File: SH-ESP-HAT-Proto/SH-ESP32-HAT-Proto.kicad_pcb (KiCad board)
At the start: 2 copper layers, 83 x 55.5 mm, 459 parts, among them J301 Conn_01x02, J302 GPIO, J304 Conn_01x02, J306 Conn_01x04, J307 GPIO, P301 Conn_01x01_Male, P302 Conn_01x01_Male, P303 Conn_01x01_Male, P304 Conn_01x01_Male, P305 Conn_01x01_Male, P306 Conn_01x01_Male, P307 Conn_01x01_Male, P308 Conn_01x01_Male, P309 Conn_01x01_Male, P310 Conn_01x01_Male, P311 Conn_01x01_Male, P312 Conn_01x01_Male, P313 Conn_01x01_Male, P314 Conn_01x01_Male, P315 Conn_01x01_Male, P316 Conn_01x01_Male, P317 Conn_01x01_Male, P319 Conn_01x01_Male, P320 Conn_01x01_Male, P322 Conn_01x01_Male, P323 Conn_01x01_Male, P324 Conn_01x01_Male, P325 Conn_01x01_Male, P326 Conn_01x01_Male, P327 Conn_01x01_Male, P328 Conn_01x01_Male, P329 Conn_01x01_Male, P330 Conn_01x01_Male

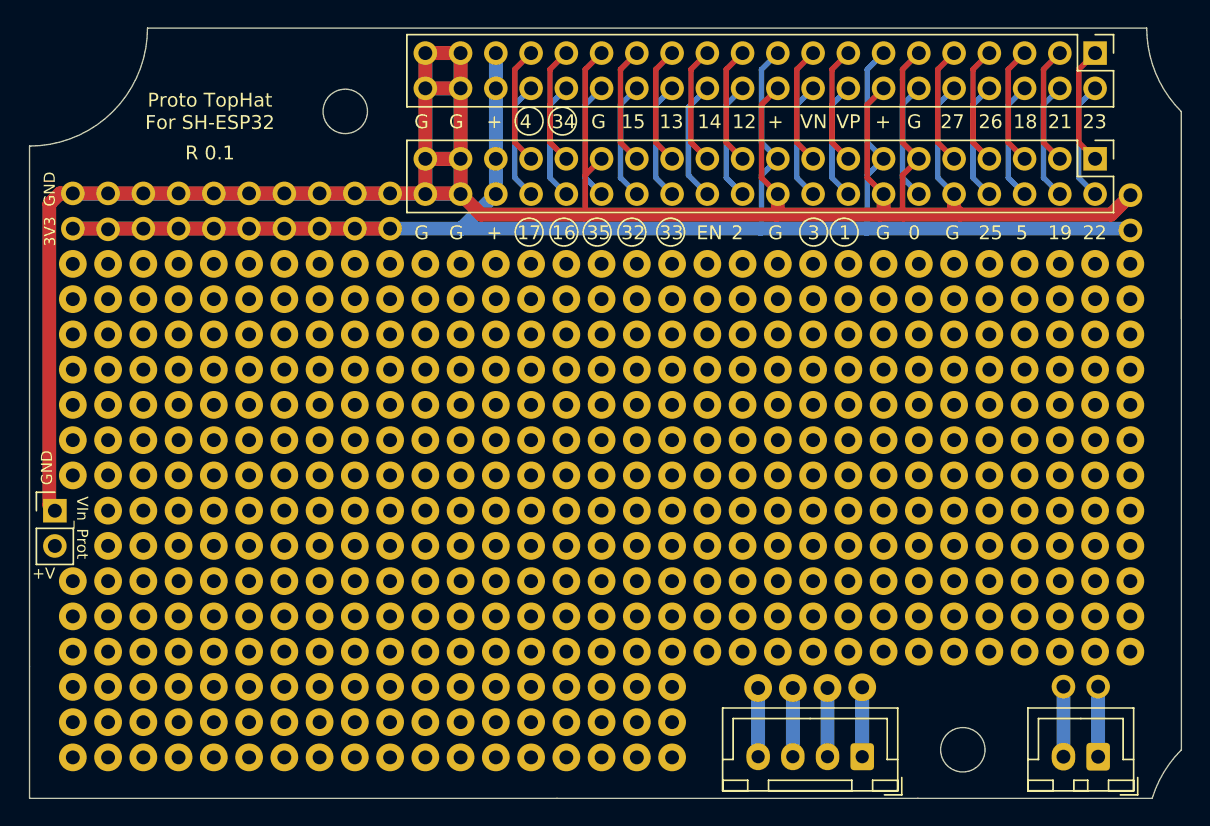
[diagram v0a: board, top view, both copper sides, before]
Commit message: Update HAT-Proto to V0.3  Pin header locs and fix outline for box corners
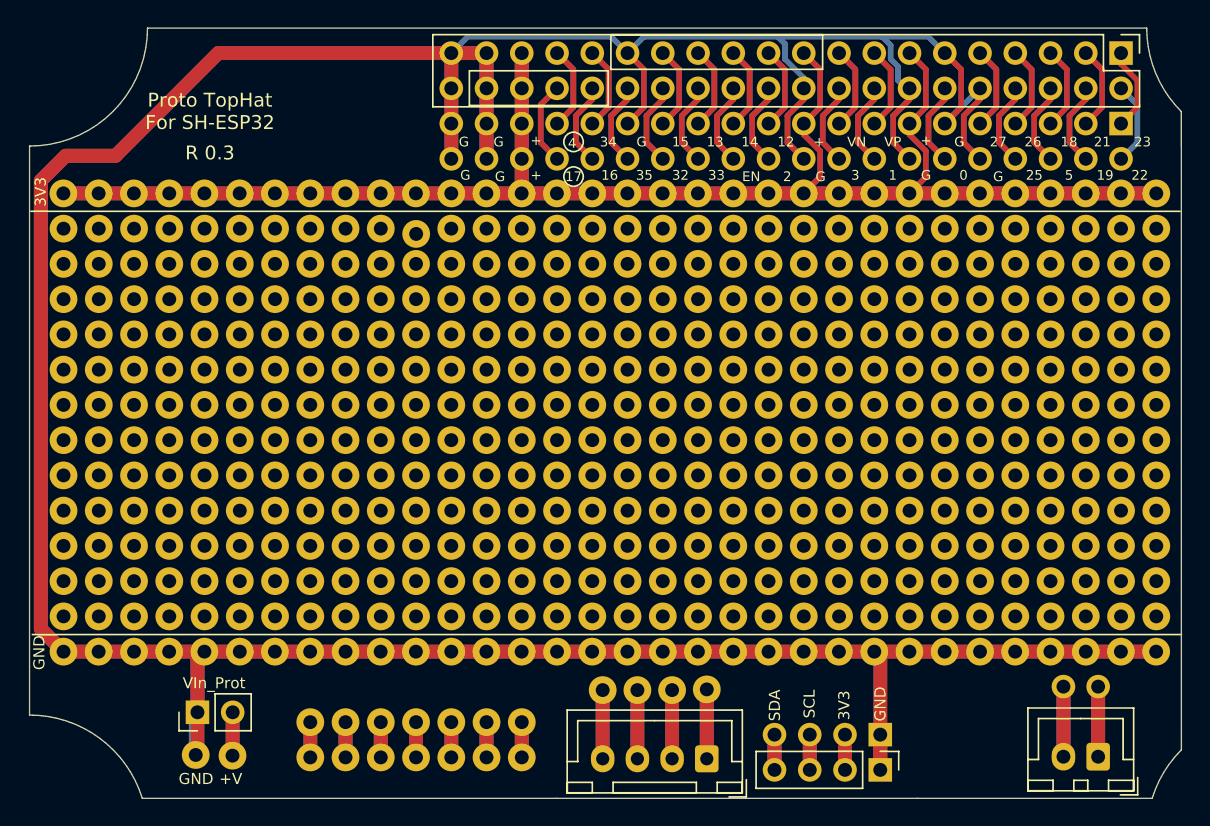
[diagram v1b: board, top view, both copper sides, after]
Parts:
- removed P307, P308, P309, P310, P311, P312, P313, P314, P315, P316, P317, P319, P320, P322, P323, P324, P325, P326, P327, P328, P329, P330: Conn_01x01_Male, ESP32-HAT:ProtoPad-Drill1mm
- removed the REF** at (97.2, 107.1)
- removed the REF** at (158.2, 102.0)
- removed the REF** at (145.5, 102.0)
- removed the REF** at (148.0, 102.0)
- removed the REF** at (153.1, 102.0)
- removed the REF** at (150.5, 102.0)
- removed the REF** at (142.9, 102.0)
- removed the REF** at (165.8, 102.0)
- removed the REF** at (99.7, 102.0)
- removed the REF** at (94.7, 102.0)
- removed the REF** at (102.3, 102.0)
- removed the REF** at (92.1, 102.0)
- removed the REF** at (163.2, 102.0)
- removed the REF** at (97.2, 102.0)
- removed the REF** at (155.6, 102.0)
- removed the REF** at (160.7, 102.0)
- removed the REF** at (125.1, 99.4)
- removed the REF** at (117.5, 99.4)
- removed the REF** at (122.6, 99.4)
- removed the REF** at (137.8, 99.4)
- removed the REF** at (135.3, 99.4)
- removed the REF** at (104.8, 109.6)
- removed the REF** at (120.1, 99.4)
- removed the REF** at (127.7, 99.4)
- removed the REF** at (130.2, 99.4)
- removed the REF** at (115.0, 99.4)
- removed the REF** at (112.4, 99.4)
- removed the REF** at (104.8, 99.4)
- removed the REF** at (109.9, 99.4)
- removed the REF** at (132.8, 99.4)
- removed the REF** at (140.4, 99.4)
- removed the REF** at (107.4, 99.4)
- removed the REF** at (158.2, 99.4)
- removed the REF** at (145.5, 99.4)
- removed the REF** at (148.0, 99.4)
- removed the REF** at (153.1, 99.4)
- removed the REF** at (150.5, 99.4)
- removed the REF** at (142.9, 99.4)
- removed the REF** at (165.8, 99.4)
- removed the REF** at (99.7, 99.4)
- removed the REF** at (94.7, 99.4)
- removed the REF** at (102.3, 99.4)
- removed the REF** at (132.8, 109.6)
- removed the REF** at (92.1, 99.4)
- removed the REF** at (163.2, 99.4)
- removed the REF** at (97.2, 99.4)
- removed the REF** at (155.6, 99.4)
- removed the REF** at (160.7, 99.4)
- removed the REF** at (125.1, 96.9)
- removed the REF** at (117.5, 96.9)
- removed the REF** at (122.6, 96.9)
- removed the REF** at (137.8, 96.9)
- removed the REF** at (135.3, 96.9)
- removed the REF** at (120.1, 96.9)
- removed the REF** at (127.7, 96.9)
- removed the REF** at (130.2, 96.9)
- removed the REF** at (115.0, 96.9)
- removed the REF** at (112.4, 96.9)
- removed the REF** at (104.8, 96.9)
- removed the REF** at (109.9, 96.9)
- removed the REF** at (132.8, 96.9)
- removed the REF** at (140.4, 96.9)
- removed the REF** at (107.4, 96.9)
- removed the REF** at (158.2, 96.9)
- removed the REF** at (145.5, 96.9)
- removed the REF** at (148.0, 96.9)
- removed the REF** at (153.1, 96.9)
- removed the REF** at (150.5, 96.9)
- removed the REF** at (142.9, 96.9)
- removed the REF** at (165.8, 96.9)
- removed the REF** at (99.7, 96.9)
- removed the REF** at (94.7, 96.9)
- removed the REF** at (102.3, 96.9)
- removed the REF** at (135.3, 109.6)
- removed the REF** at (92.1, 96.9)
- removed the REF** at (163.2, 96.9)
- removed the REF** at (97.2, 96.9)
- removed the REF** at (155.6, 96.9)
- removed the REF** at (160.7, 96.9)
- removed the REF** at (125.1, 94.4)
- removed the REF** at (117.5, 94.4)
- removed the REF** at (122.6, 94.4)
- removed the REF** at (137.8, 94.4)
- removed the REF** at (135.3, 94.4)
- removed the REF** at (120.1, 94.4)
- removed the REF** at (127.7, 94.4)
- removed the REF** at (130.2, 94.4)
- removed the REF** at (115.0, 94.4)
- removed the REF** at (112.4, 94.4)
- removed the REF** at (104.8, 94.4)
- removed the REF** at (109.9, 94.4)
- removed the REF** at (132.8, 94.4)
- removed the REF** at (140.4, 94.4)
- removed the REF** at (107.4, 94.4)
- removed the REF** at (130.2, 109.6)
- removed the REF** at (158.2, 94.4)
- removed the REF** at (145.5, 94.4)
- removed the REF** at (148.0, 94.4)
- removed the REF** at (153.1, 94.4)
- removed the REF** at (150.5, 94.4)
- removed the REF** at (142.9, 94.4)
- removed the REF** at (165.8, 94.4)
- removed the REF** at (99.7, 94.4)
- removed the REF** at (94.7, 94.4)
- removed the REF** at (102.3, 94.4)
- removed the REF** at (92.1, 107.1)
- removed the REF** at (127.7, 109.6)
- removed the REF** at (163.2, 94.4)
- removed the REF** at (97.2, 94.4)
- removed the REF** at (155.6, 94.4)
- removed the REF** at (160.7, 94.4)
- removed the REF** at (125.1, 91.8)
- removed the REF** at (117.5, 91.8)
- removed the REF** at (122.6, 91.8)
- removed the REF** at (137.8, 91.8)
- removed the REF** at (135.3, 91.8)
- removed the REF** at (120.1, 91.8)
- removed the REF** at (125.1, 109.6)
- removed the REF** at (127.7, 91.8)
- removed the REF** at (130.2, 91.8)
- removed the REF** at (115.0, 91.8)
- removed the REF** at (112.4, 91.8)
- removed the REF** at (104.8, 91.8)
- removed the REF** at (109.9, 91.8)
- removed the REF** at (132.8, 91.8)
- removed the REF** at (140.4, 91.8)
- removed the REF** at (107.4, 91.8)
- removed the REF** at (158.2, 91.8)
- removed the REF** at (99.7, 109.6)
- removed the REF** at (145.5, 91.8)
- removed the REF** at (148.0, 91.8)
- removed the REF** at (153.1, 91.8)
- removed the REF** at (150.5, 91.8)
- removed the REF** at (142.9, 91.8)
- removed the REF** at (165.8, 91.8)
- removed the REF** at (99.7, 91.8)
- removed the REF** at (94.7, 91.8)
- removed the REF** at (102.3, 91.8)
- removed the REF** at (163.2, 91.8)
- removed the REF** at (97.2, 91.8)
- removed the REF** at (155.6, 91.8)
- removed the REF** at (160.7, 91.8)
- removed the REF** at (125.1, 89.3)
- removed the REF** at (117.5, 89.3)
- removed the REF** at (122.6, 89.3)
- removed the REF** at (137.8, 89.3)
- removed the REF** at (135.3, 89.3)
- removed the REF** at (120.1, 89.3)
- removed the REF** at (127.7, 89.3)
- removed the REF** at (130.2, 89.3)
- removed the REF** at (115.0, 89.3)
- removed the REF** at (112.4, 89.3)
- removed the REF** at (104.8, 89.3)
- removed the REF** at (109.9, 89.3)
- removed the REF** at (132.8, 89.3)
- removed the REF** at (140.4, 89.3)
- removed the REF** at (107.4, 89.3)
- removed the REF** at (158.2, 89.3)
- removed the REF** at (145.5, 89.3)
- removed the REF** at (94.7, 109.6)
- removed the REF** at (148.0, 89.3)
- removed the REF** at (153.1, 89.3)
- removed the REF** at (150.5, 89.3)
- removed the REF** at (142.9, 89.3)
- removed the REF** at (165.8, 89.3)
- removed the REF** at (99.7, 89.3)
- removed the REF** at (94.7, 89.3)
- removed the REF** at (102.3, 89.3)
- removed the REF** at (92.1, 89.3)
- removed the REF** at (163.2, 89.3)
- removed the REF** at (102.3, 109.6)
- removed the REF** at (97.2, 89.3)
- removed the REF** at (155.6, 89.3)
- removed the REF** at (160.7, 89.3)
- removed the REF** at (125.1, 86.7)
- removed the REF** at (117.5, 86.7)
- removed the REF** at (122.6, 86.7)
- removed the REF** at (137.8, 86.7)
- removed the REF** at (135.3, 86.7)
- removed the REF** at (120.1, 86.7)
- removed the REF** at (127.7, 86.7)
- removed the REF** at (92.1, 109.6)
- removed the REF** at (130.2, 86.7)
- removed the REF** at (115.0, 86.7)
- removed the REF** at (112.4, 86.7)
- removed the REF** at (104.8, 86.7)
- removed the REF** at (109.9, 86.7)
- removed the REF** at (132.8, 86.7)
- removed the REF** at (140.4, 86.7)
- removed the REF** at (107.4, 86.7)
- removed the REF** at (158.2, 86.7)
- removed the REF** at (145.5, 86.7)
- removed the REF** at (97.2, 109.6)
- removed the REF** at (148.0, 86.7)
- removed the REF** at (153.1, 86.7)
- removed the REF** at (150.5, 86.7)
- removed the REF** at (142.9, 86.7)
- removed the REF** at (165.8, 86.7)
- removed the REF** at (99.7, 86.7)
- removed the REF** at (102.3, 86.7)
- removed the REF** at (163.2, 86.7)
- removed the REF** at (155.6, 86.7)
- removed the REF** at (160.7, 86.7)
- removed the REF** at (125.1, 107.1)
- removed the REF** at (125.1, 84.2)
- removed the REF** at (117.5, 84.2)
- removed the REF** at (122.6, 84.2)
- removed the REF** at (137.8, 84.2)
- removed the REF** at (135.3, 84.2)
- removed the REF** at (120.1, 84.2)
- removed the REF** at (127.7, 84.2)
- removed the REF** at (130.2, 84.2)
- removed the REF** at (115.0, 84.2)
- removed the REF** at (112.4, 84.2)
- removed the REF** at (102.3, 107.1)
- removed the REF** at (104.8, 84.2)
- removed the REF** at (109.9, 84.2)
- removed the REF** at (132.8, 84.2)
- removed the REF** at (140.4, 84.2)
- removed the REF** at (107.4, 84.2)
- removed the REF** at (158.2, 84.2)
- removed the REF** at (145.5, 84.2)
- removed the REF** at (148.0, 84.2)
- removed the REF** at (153.1, 84.2)
- removed the REF** at (150.5, 84.2)
- removed the REF** at (142.9, 84.2)
- removed the REF** at (165.8, 84.2)
- removed the REF** at (99.7, 84.2)
- removed the REF** at (102.3, 84.2)
- removed the REF** at (163.2, 84.2)
- removed the REF** at (155.6, 84.2)
- removed the REF** at (160.7, 84.2)
- removed the REF** at (125.1, 81.7)
- removed the REF** at (117.5, 81.7)
- removed the REF** at (122.6, 81.7)
- removed the REF** at (135.3, 107.1)
- removed the REF** at (137.8, 81.7)
- removed the REF** at (135.3, 81.7)
- removed the REF** at (120.1, 81.7)
- removed the REF** at (127.7, 81.7)
- removed the REF** at (130.2, 81.7)
- removed the REF** at (115.0, 81.7)
- removed the REF** at (112.4, 81.7)
- removed the REF** at (104.8, 81.7)
- removed the REF** at (109.9, 81.7)
- removed the REF** at (132.8, 81.7)
- removed the REF** at (140.4, 81.7)
- removed the REF** at (107.4, 81.7)
- removed the REF** at (158.2, 81.7)
- removed the REF** at (145.5, 81.7)
- removed the REF** at (148.0, 81.7)
- removed the REF** at (153.1, 81.7)
- removed the REF** at (150.5, 81.7)
- removed the REF** at (142.9, 81.7)
- removed the REF** at (165.8, 81.7)
- removed the REF** at (99.7, 81.7)
- removed the REF** at (127.7, 107.1)
- removed the REF** at (102.3, 81.7)
- removed the REF** at (163.2, 81.7)
- removed the REF** at (155.6, 81.7)
- removed the REF** at (160.7, 81.7)
- removed the REF** at (125.1, 79.1)
- removed the REF** at (117.5, 79.1)
- removed the REF** at (122.6, 79.1)
- removed the REF** at (137.8, 79.1)
- removed the REF** at (135.3, 79.1)
- removed the REF** at (120.1, 79.1)
- removed the REF** at (130.2, 107.1)
- removed the REF** at (127.7, 79.1)
- removed the REF** at (130.2, 79.1)
- removed the REF** at (115.0, 79.1)
- removed the REF** at (112.4, 79.1)
- removed the REF** at (104.8, 79.1)
- removed the REF** at (109.9, 79.1)
- removed the REF** at (132.8, 79.1)
- removed the REF** at (140.4, 79.1)
- removed the REF** at (107.4, 79.1)
- removed the REF** at (158.2, 79.1)
- removed the REF** at (145.5, 79.1)
- removed the REF** at (148.0, 79.1)
- removed the REF** at (153.1, 79.1)
- removed the REF** at (150.5, 79.1)
- removed the REF** at (142.9, 79.1)
- removed the REF** at (165.8, 79.1)
- removed the REF** at (99.7, 79.1)
- removed the REF** at (102.3, 79.1)
- removed the REF** at (163.2, 79.1)
- removed the REF** at (155.6, 79.1)
- removed the REF** at (112.4, 104.5)
- removed the REF** at (160.7, 79.1)
- removed the REF** at (125.1, 76.6)
- removed the REF** at (117.5, 76.6)
- removed the REF** at (122.6, 76.6)
- removed the REF** at (137.8, 76.6)
- removed the REF** at (135.3, 76.6)
- removed the REF** at (120.1, 76.6)
- removed the REF** at (127.7, 76.6)
- removed the REF** at (130.2, 76.6)
- removed the REF** at (115.0, 76.6)
- removed the REF** at (104.8, 104.5)
- removed the REF** at (112.4, 76.6)
- removed the REF** at (104.8, 76.6)
- removed the REF** at (109.9, 76.6)
- removed the REF** at (132.8, 76.6)
- removed the REF** at (140.4, 76.6)
- removed the REF** at (107.4, 76.6)
- removed the REF** at (158.2, 76.6)
- removed the REF** at (145.5, 76.6)
- removed the REF** at (148.0, 76.6)
- removed the REF** at (153.1, 76.6)
- removed the REF** at (109.9, 104.5)
- removed the REF** at (150.5, 76.6)
- removed the REF** at (142.9, 76.6)
- removed the REF** at (165.8, 76.6)
- removed the REF** at (99.7, 76.6)
- removed the REF** at (102.3, 76.6)
- removed the REF** at (163.2, 76.6)
- removed the REF** at (155.6, 76.6)
- removed the REF** at (160.7, 76.6)
- removed the REF** at (102.3, 74.0)
- removed the REF** at (99.7, 74.0)
- removed the REF** at (94.7, 107.1)
- removed the REF** at (132.8, 104.5)
- removed the REF** at (107.4, 74.0)
- removed the REF** at (115.0, 74.0)
- removed the REF** at (112.4, 74.0)
- removed the REF** at (104.8, 74.0)
- removed the REF** at (109.9, 74.0)
- removed the REF** at (120.1, 74.0)
- removed the REF** at (127.7, 74.0)
- removed the REF** at (125.1, 74.0)
- removed the REF** at (117.5, 74.0)
- removed the REF** at (122.6, 74.0)
- removed the REF** at (107.4, 104.5)
- removed the REF** at (132.8, 74.0)
- removed the REF** at (140.4, 74.0)
- removed the REF** at (137.8, 74.0)
- removed the REF** at (130.2, 74.0)
- removed the REF** at (135.3, 74.0)
- removed the REF** at (145.5, 74.0)
- removed the REF** at (153.1, 74.0)
- removed the REF** at (150.5, 74.0)
- removed the REF** at (142.9, 74.0)
- removed the REF** at (148.0, 74.0)
- removed the REF** at (122.6, 104.5)
- removed the REF** at (155.6, 74.0)
- removed the REF** at (158.2, 74.0)
- removed the REF** at (160.7, 74.0)
- removed the REF** at (163.2, 74.0)
- removed the REF** at (165.8, 74.0)
- removed the REF** at (135.3, 104.5)
- removed the REF** at (120.1, 104.5)
- removed the REF** at (130.2, 104.5)
- removed the REF** at (127.7, 104.5)
- removed the REF** at (125.1, 104.5)
- removed the REF** at (99.7, 104.5)
- removed the REF** at (115.0, 104.5)
- removed the REF** at (99.7, 107.1)
- removed the REF** at (117.5, 104.5)
- removed the REF** at (94.7, 104.5)
- removed the REF** at (102.3, 104.5)
- removed the REF** at (92.1, 104.5)
- removed the REF** at (97.2, 104.5)
- removed the REF** at (168.3, 102.0)
- removed the REF** at (168.3, 74.0)
- removed the REF** at (97.2, 79.1)
- removed the REF** at (97.2, 74.0)
- removed the REF** at (92.1, 74.0)
- removed the REF** at (132.8, 107.1)
- removed the REF** at (97.2, 86.7)
- removed the REF** at (92.1, 86.7)
- removed the REF** at (94.7, 86.7)
- removed the REF** at (92.1, 79.1)
- removed the REF** at (94.7, 74.0)
- removed the REF** at (94.7, 79.1)
- removed the REF** at (97.2, 76.6)
- removed the REF** at (92.1, 76.6)
- removed the REF** at (94.7, 76.6)
- removed the REF** at (97.2, 81.7)
- removed the REF** at (92.1, 81.7)
- removed the REF** at (94.7, 81.7)
- removed the REF** at (97.2, 84.2)
- removed the REF** at (92.1, 84.2)
- removed the REF** at (94.7, 84.2)
- removed the REF** at (125.1, 102.0)
- removed the REF** at (117.5, 102.0)
- removed the REF** at (122.6, 102.0)
- removed the REF** at (137.8, 102.0)
- removed the REF** at (135.3, 102.0)
- removed the REF** at (104.8, 107.1)
- removed the REF** at (120.1, 102.0)
- removed the REF** at (127.7, 102.0)
- removed the REF** at (130.2, 102.0)
- removed the REF** at (115.0, 102.0)
- removed the REF** at (112.4, 102.0)
- removed the REF** at (104.8, 102.0)
- removed the REF** at (109.9, 102.0)
- removed the REF** at (132.8, 102.0)
- removed the REF** at (140.4, 102.0)
- removed the REF** at (107.4, 102.0)
- added J303: I2C, Connector_PinHeader_2.54mm:PinHeader_1x04_P2.54mm_Vertical, B.Cu at (150.3, 107.9)
- added J305: I2C, Connector_PinHeader_2.54mm:PinHeader_1x04_P2.54mm_Vertical, F.Cu at (150.3, 110.5)
- added P321: Conn_01x01_Male, ESP32-HAT:ProtoPad-Drill1mm, F.Cu at (101.0, 109.4)
- added P331: Conn_01x01_Male, ESP32-HAT:ProtoPad-Drill1mm, F.Cu at (103.6, 109.5)
- added REF**: ProtoPad-Drill1mm, ESP32-HAT:ProtoPad-Drill1mm, F.Cu at (94.0, 102.0)
- added REF**: ProtoPad-Drill1mm, ESP32-HAT:ProtoPad-Drill1mm, F.Cu at (94.0, 94.4)
- added REF**: ProtoPad-Drill1mm, ESP32-HAT:ProtoPad-Drill1mm, F.Cu at (116.8, 102.0)
- added REF**: ProtoPad-Drill1mm, ESP32-HAT:ProtoPad-Drill1mm, F.Cu at (119.4, 102.0)
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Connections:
- J304 pad 2: (no net) -> /IOHeader/Vin_protected
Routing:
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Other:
- outline, holes or cut-outs redrawn
- board text added: "R 0.3"
- board text added: "SCL"
- board text added: "SDA"
- board text removed: "R 0.1"

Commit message: Change 'unconnected' holes to Square pads - Fixed DRC errors
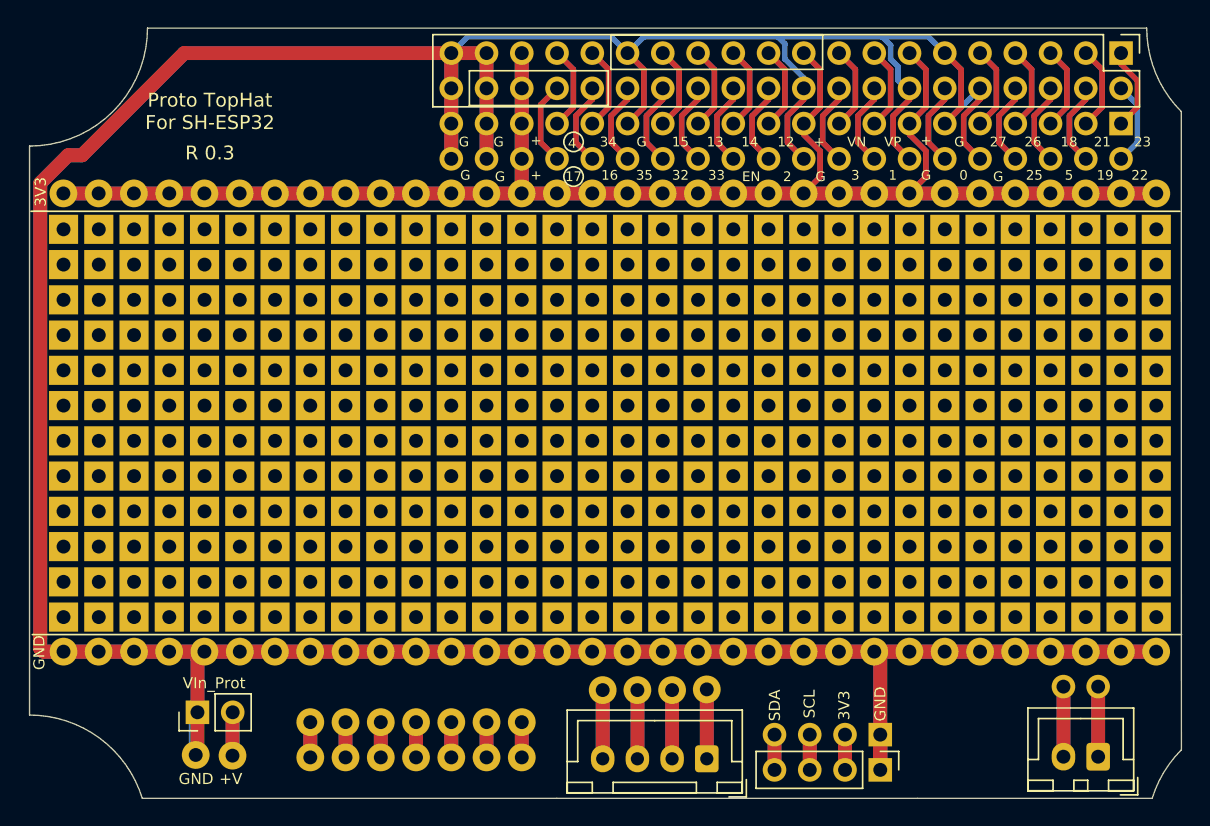
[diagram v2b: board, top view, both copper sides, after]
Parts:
- removed the REF** at (94.0, 94.4)
- removed the REF** at (162.6, 71.5)
- removed the REF** at (157.5, 71.5)
- removed the REF** at (165.1, 71.5)
- removed the REF** at (167.7, 71.5)
- removed the REF** at (144.8, 71.5)
- removed the REF** at (152.4, 71.5)
- removed the REF** at (154.9, 71.5)
- removed the REF** at (149.9, 71.5)
- removed the REF** at (91.5, 76.6)
- removed the REF** at (147.3, 71.5)
- removed the REF** at (160.0, 71.5)
- removed the REF** at (142.2, 71.5)
- removed the REF** at (134.6, 71.5)
- removed the REF** at (132.1, 71.5)
- removed the REF** at (129.6, 71.5)
- removed the REF** at (121.9, 71.5)
- removed the REF** at (137.2, 71.5)
- removed the REF** at (139.7, 71.5)
- removed the REF** at (124.5, 71.5)
- removed the REF** at (91.5, 79.1)
- removed the REF** at (119.4, 71.5)
- removed the REF** at (127.0, 71.5)
- removed the REF** at (109.2, 107.1)
- removed the REF** at (111.8, 107.1)
- removed the REF** at (114.3, 107.1)
- removed the REF** at (114.3, 109.6)
- removed the REF** at (111.8, 109.6)
- removed the REF** at (109.2, 109.6)
- removed the REF** at (124.5, 109.6)
- removed the REF** at (121.9, 109.6)
- removed the REF** at (91.5, 86.7)
- removed the REF** at (116.8, 109.6)
- removed the REF** at (119.4, 109.6)
- removed the REF** at (119.4, 107.1)
- removed the REF** at (124.5, 107.1)
- removed the REF** at (121.9, 107.1)
- removed the REF** at (116.8, 107.1)
- removed the REF** at (170.2, 96.9)
- removed the REF** at (170.2, 84.2)
- removed the REF** at (170.2, 91.8)
- removed the REF** at (170.2, 81.7)
- removed the REF** at (170.2, 76.6)
- removed the REF** at (170.2, 89.3)
- removed the REF** at (170.2, 86.7)
- removed the REF** at (170.2, 99.4)
- removed the REF** at (170.2, 94.4)
- removed the REF** at (170.2, 79.1)
- removed the REF** at (99.1, 79.1)
- removed the REF** at (99.1, 86.7)
- removed the REF** at (94.0, 86.7)
- removed the REF** at (96.5, 86.7)
- removed the REF** at (91.5, 74.0)
- removed the REF** at (94.0, 79.1)
- removed the REF** at (96.5, 79.1)
- removed the REF** at (99.1, 76.6)
- removed the REF** at (94.0, 76.6)
- removed the REF** at (96.5, 76.6)
- removed the REF** at (99.1, 81.7)
- removed the REF** at (94.0, 81.7)
- removed the REF** at (96.5, 81.7)
- removed the REF** at (99.1, 84.2)
- removed the REF** at (94.0, 84.2)
- removed the REF** at (91.5, 89.3)
- removed the REF** at (96.5, 84.2)
- removed the REF** at (127.0, 99.4)
- removed the REF** at (119.4, 99.4)
- removed the REF** at (124.5, 99.4)
- removed the REF** at (139.7, 99.4)
- removed the REF** at (137.2, 99.4)
- removed the REF** at (121.9, 99.4)
- removed the REF** at (129.6, 99.4)
- removed the REF** at (132.1, 99.4)
- removed the REF** at (116.8, 99.4)
- removed the REF** at (91.5, 84.2)
- removed the REF** at (114.3, 99.4)
- removed the REF** at (106.7, 99.4)
- removed the REF** at (111.8, 99.4)
- removed the REF** at (134.6, 99.4)
- removed the REF** at (142.2, 99.4)
- removed the REF** at (109.2, 99.4)
- removed the REF** at (160.0, 99.4)
- removed the REF** at (147.3, 99.4)
- removed the REF** at (149.9, 99.4)
- removed the REF** at (154.9, 99.4)
- removed the REF** at (91.5, 81.7)
- removed the REF** at (152.4, 99.4)
- removed the REF** at (144.8, 99.4)
- removed the REF** at (167.7, 99.4)
- removed the REF** at (101.6, 99.4)
- removed the REF** at (96.5, 99.4)
- removed the REF** at (104.2, 99.4)
- removed the REF** at (165.1, 99.4)
- removed the REF** at (99.1, 99.4)
- removed the REF** at (157.5, 99.4)
- removed the REF** at (162.6, 99.4)
- removed the REF** at (96.5, 71.5)
- removed the REF** at (127.0, 96.9)
- removed the REF** at (119.4, 96.9)
- removed the REF** at (124.5, 96.9)
- removed the REF** at (139.7, 96.9)
- removed the REF** at (137.2, 96.9)
- removed the REF** at (121.9, 96.9)
- removed the REF** at (129.6, 96.9)
- removed the REF** at (132.1, 96.9)
- removed the REF** at (116.8, 96.9)
- removed the REF** at (114.3, 96.9)
- removed the REF** at (106.7, 96.9)
- removed the REF** at (111.8, 96.9)
- removed the REF** at (134.6, 96.9)
- removed the REF** at (142.2, 96.9)
- removed the REF** at (109.2, 96.9)
- removed the REF** at (160.0, 96.9)
- removed the REF** at (147.3, 96.9)
- removed the REF** at (149.9, 96.9)
- removed the REF** at (154.9, 96.9)
- removed the REF** at (152.4, 96.9)
- removed the REF** at (99.1, 71.5)
- removed the REF** at (144.8, 96.9)
- removed the REF** at (167.7, 96.9)
- removed the REF** at (101.6, 96.9)
- removed the REF** at (96.5, 96.9)
- removed the REF** at (104.2, 96.9)
- removed the REF** at (165.1, 96.9)
- removed the REF** at (99.1, 96.9)
- removed the REF** at (157.5, 96.9)
- removed the REF** at (162.6, 96.9)
- removed the REF** at (127.0, 94.4)
- removed the REF** at (96.5, 74.0)
- removed the REF** at (119.4, 94.4)
- removed the REF** at (124.5, 94.4)
- removed the REF** at (139.7, 94.4)
- removed the REF** at (137.2, 94.4)
- removed the REF** at (121.9, 94.4)
- removed the REF** at (129.6, 94.4)
- removed the REF** at (132.1, 94.4)
- removed the REF** at (116.8, 94.4)
- removed the REF** at (114.3, 94.4)
- removed the REF** at (106.7, 94.4)
- removed the REF** at (94.0, 74.0)
- removed the REF** at (111.8, 94.4)
- removed the REF** at (134.6, 94.4)
- removed the REF** at (142.2, 94.4)
- removed the REF** at (109.2, 94.4)
- removed the REF** at (160.0, 94.4)
- removed the REF** at (147.3, 94.4)
- removed the REF** at (149.9, 94.4)
- removed the REF** at (154.9, 94.4)
- removed the REF** at (152.4, 94.4)
- removed the REF** at (144.8, 94.4)
- removed the REF** at (99.1, 74.0)
- removed the REF** at (167.7, 94.4)
- removed the REF** at (101.6, 94.4)
- removed the REF** at (96.5, 94.4)
- removed the REF** at (104.2, 94.4)
- removed the REF** at (165.1, 94.4)
- removed the REF** at (99.1, 94.4)
- removed the REF** at (157.5, 94.4)
- removed the REF** at (162.6, 94.4)
- removed the REF** at (127.0, 91.8)
- removed the REF** at (119.4, 91.8)
- removed the REF** at (104.2, 71.5)
- removed the REF** at (124.5, 91.8)
- removed the REF** at (139.7, 91.8)
- removed the REF** at (137.2, 91.8)
- removed the REF** at (121.9, 91.8)
- removed the REF** at (129.6, 91.8)
- removed the REF** at (132.1, 91.8)
- removed the REF** at (116.8, 91.8)
- removed the REF** at (114.3, 91.8)
- removed the REF** at (106.7, 91.8)
- removed the REF** at (111.8, 91.8)
- removed the REF** at (101.6, 71.5)
- removed the REF** at (134.6, 91.8)
- removed the REF** at (142.2, 91.8)
- removed the REF** at (109.2, 91.8)
- removed the REF** at (160.0, 91.8)
- removed the REF** at (147.3, 91.8)
- removed the REF** at (149.9, 91.8)
- removed the REF** at (154.9, 91.8)
- removed the REF** at (152.4, 91.8)
- removed the REF** at (144.8, 91.8)
- removed the REF** at (167.7, 91.8)
- removed the REF** at (109.2, 71.5)
- removed the REF** at (101.6, 91.8)
- removed the REF** at (96.5, 91.8)
- removed the REF** at (104.2, 91.8)
- removed the REF** at (165.1, 91.8)
- removed the REF** at (99.1, 91.8)
- removed the REF** at (157.5, 91.8)
- removed the REF** at (162.6, 91.8)
- removed the REF** at (127.0, 89.3)
- removed the REF** at (119.4, 89.3)
- removed the REF** at (124.5, 89.3)
- removed the REF** at (111.8, 71.5)
- removed the REF** at (139.7, 89.3)
- removed the REF** at (137.2, 89.3)
- removed the REF** at (121.9, 89.3)
- removed the REF** at (129.6, 89.3)
- removed the REF** at (132.1, 89.3)
- removed the REF** at (116.8, 89.3)
- removed the REF** at (114.3, 89.3)
- removed the REF** at (106.7, 89.3)
- removed the REF** at (111.8, 89.3)
- removed the REF** at (134.6, 89.3)
- removed the REF** at (106.7, 71.5)
- removed the REF** at (142.2, 89.3)
- removed the REF** at (109.2, 89.3)
- removed the REF** at (160.0, 89.3)
- removed the REF** at (147.3, 89.3)
- removed the REF** at (149.9, 89.3)
- removed the REF** at (154.9, 89.3)
- removed the REF** at (152.4, 89.3)
- removed the REF** at (144.8, 89.3)
- removed the REF** at (167.7, 89.3)
- removed the REF** at (101.6, 89.3)
- removed the REF** at (91.5, 96.9)
- removed the REF** at (114.3, 71.5)
- removed the REF** at (96.5, 89.3)
- removed the REF** at (104.2, 89.3)
- removed the REF** at (94.0, 89.3)
- removed the REF** at (165.1, 89.3)
- removed the REF** at (99.1, 89.3)
- removed the REF** at (157.5, 89.3)
- removed the REF** at (162.6, 89.3)
- removed the REF** at (127.0, 86.7)
- removed the REF** at (119.4, 86.7)
- removed the REF** at (124.5, 86.7)
- removed the REF** at (104.2, 74.0)
- removed the REF** at (139.7, 86.7)
- removed the REF** at (137.2, 86.7)
- removed the REF** at (121.9, 86.7)
- removed the REF** at (129.6, 86.7)
- removed the REF** at (132.1, 86.7)
- removed the REF** at (116.8, 86.7)
- removed the REF** at (114.3, 86.7)
- removed the REF** at (106.7, 86.7)
- removed the REF** at (111.8, 86.7)
- removed the REF** at (134.6, 86.7)
- removed the REF** at (101.6, 74.0)
- removed the REF** at (142.2, 86.7)
- removed the REF** at (109.2, 86.7)
- removed the REF** at (160.0, 86.7)
- removed the REF** at (147.3, 86.7)
- removed the REF** at (149.9, 86.7)
- removed the REF** at (154.9, 86.7)
- removed the REF** at (152.4, 86.7)
- removed the REF** at (144.8, 86.7)
- removed the REF** at (167.7, 86.7)
- removed the REF** at (101.6, 86.7)
- removed the REF** at (109.2, 74.0)
- removed the REF** at (104.2, 86.7)
- removed the REF** at (165.1, 86.7)
- removed the REF** at (157.5, 86.7)
- removed the REF** at (162.6, 86.7)
- removed the REF** at (127.0, 84.2)
- removed the REF** at (119.4, 84.2)
- removed the REF** at (124.5, 84.2)
- removed the REF** at (139.7, 84.2)
- removed the REF** at (137.2, 84.2)
- removed the REF** at (121.9, 84.2)
- removed the REF** at (111.8, 74.0)
- removed the REF** at (129.6, 84.2)
- removed the REF** at (132.1, 84.2)
- removed the REF** at (116.8, 84.2)
- removed the REF** at (114.3, 84.2)
- removed the REF** at (106.7, 84.2)
- removed the REF** at (111.8, 84.2)
- removed the REF** at (134.6, 84.2)
- removed the REF** at (142.2, 84.2)
- removed the REF** at (109.2, 84.2)
- removed the REF** at (160.0, 84.2)
- removed the REF** at (106.7, 74.0)
- removed the REF** at (147.3, 84.2)
- removed the REF** at (149.9, 84.2)
- removed the REF** at (154.9, 84.2)
- removed the REF** at (152.4, 84.2)
- removed the REF** at (144.8, 84.2)
- removed the REF** at (167.7, 84.2)
- removed the REF** at (101.6, 84.2)
- removed the REF** at (104.2, 84.2)
- removed the REF** at (165.1, 84.2)
- removed the REF** at (157.5, 84.2)
- removed the REF** at (114.3, 74.0)
- removed the REF** at (162.6, 84.2)
- removed the REF** at (127.0, 81.7)
- removed the REF** at (119.4, 81.7)
- removed the REF** at (124.5, 81.7)
- removed the REF** at (139.7, 81.7)
- removed the REF** at (137.2, 81.7)
- removed the REF** at (121.9, 81.7)
- removed the REF** at (129.6, 81.7)
- removed the REF** at (132.1, 81.7)
- removed the REF** at (116.8, 81.7)
- removed the REF** at (114.3, 81.7)
- removed the REF** at (106.7, 81.7)
- removed the REF** at (111.8, 81.7)
- removed the REF** at (134.6, 81.7)
- removed the REF** at (142.2, 81.7)
- removed the REF** at (109.2, 81.7)
- removed the REF** at (160.0, 81.7)
- removed the REF** at (147.3, 81.7)
- removed the REF** at (149.9, 81.7)
- removed the REF** at (154.9, 81.7)
- removed the REF** at (152.4, 81.7)
- removed the REF** at (144.8, 81.7)
- removed the REF** at (167.7, 81.7)
- removed the REF** at (101.6, 81.7)
- removed the REF** at (104.2, 81.7)
- removed the REF** at (165.1, 81.7)
- removed the REF** at (157.5, 81.7)
- removed the REF** at (162.6, 81.7)
- removed the REF** at (127.0, 79.1)
- removed the REF** at (119.4, 79.1)
- removed the REF** at (124.5, 79.1)
- removed the REF** at (139.7, 79.1)
- removed the REF** at (137.2, 79.1)
- removed the REF** at (121.9, 79.1)
- removed the REF** at (129.6, 79.1)
- removed the REF** at (132.1, 79.1)
- removed the REF** at (116.8, 79.1)
- removed the REF** at (114.3, 79.1)
- removed the REF** at (106.7, 79.1)
- removed the REF** at (111.8, 79.1)
- removed the REF** at (91.5, 99.4)
- removed the REF** at (134.6, 79.1)
- removed the REF** at (142.2, 79.1)
- removed the REF** at (109.2, 79.1)
- removed the REF** at (160.0, 79.1)
- removed the REF** at (147.3, 79.1)
- removed the REF** at (149.9, 79.1)
- removed the REF** at (154.9, 79.1)
- removed the REF** at (152.4, 79.1)
- removed the REF** at (144.8, 79.1)
- removed the REF** at (167.7, 79.1)
- removed the REF** at (101.6, 79.1)
- removed the REF** at (104.2, 79.1)
- removed the REF** at (165.1, 79.1)
- removed the REF** at (157.5, 79.1)
- removed the REF** at (162.6, 79.1)
- removed the REF** at (127.0, 76.6)
- removed the REF** at (119.4, 76.6)
- removed the REF** at (124.5, 76.6)
- removed the REF** at (139.7, 76.6)
- removed the REF** at (137.2, 76.6)
- removed the REF** at (121.9, 76.6)
- removed the REF** at (129.6, 76.6)
- removed the REF** at (132.1, 76.6)
- removed the REF** at (116.8, 76.6)
- removed the REF** at (114.3, 76.6)
- removed the REF** at (106.7, 76.6)
- removed the REF** at (111.8, 76.6)
- removed the REF** at (134.6, 76.6)
- removed the REF** at (142.2, 76.6)
- removed the REF** at (109.2, 76.6)
- removed the REF** at (160.0, 76.6)
- removed the REF** at (147.3, 76.6)
- removed the REF** at (149.9, 76.6)
- removed the REF** at (154.9, 76.6)
- removed the REF** at (152.4, 76.6)
- removed the REF** at (144.8, 76.6)
- removed the REF** at (167.7, 76.6)
- removed the REF** at (101.6, 76.6)
- removed the REF** at (104.2, 76.6)
- removed the REF** at (165.1, 76.6)
- removed the REF** at (157.5, 76.6)
- removed the REF** at (162.6, 76.6)
- removed the REF** at (116.8, 74.0)
- removed the REF** at (121.9, 74.0)
- removed the REF** at (129.6, 74.0)
- removed the REF** at (127.0, 74.0)
- removed the REF** at (119.4, 74.0)
- removed the REF** at (124.5, 74.0)
- removed the REF** at (134.6, 74.0)
- removed the REF** at (142.2, 74.0)
- removed the REF** at (139.7, 74.0)
- removed the REF** at (132.1, 74.0)
- removed the REF** at (137.2, 74.0)
- removed the REF** at (147.3, 74.0)
- removed the REF** at (154.9, 74.0)
- removed the REF** at (152.4, 74.0)
- removed the REF** at (144.8, 74.0)
- removed the REF** at (149.9, 74.0)
- removed the REF** at (157.5, 74.0)
- removed the REF** at (160.0, 74.0)
- removed the REF** at (162.6, 74.0)
- removed the REF** at (165.1, 74.0)
- removed the REF** at (167.7, 74.0)
- removed the REF** at (91.5, 91.8)
- removed the REF** at (91.5, 94.4)
- removed the REF** at (170.2, 71.5)
- removed the REF** at (94.0, 96.9)
- removed the REF** at (170.2, 74.0)
- removed the REF** at (116.9, 71.9)
- removed the REF** at (94.0, 99.4)
- removed the REF** at (94.0, 91.8)
- added P307: Conn_01x01_Male, ESP32-HAT:ProtoPad-Drill1mm, F.Cu at (109.2, 107.1)
- added P308: Conn_01x01_Male, ESP32-HAT:ProtoPad-Drill1mm, F.Cu at (116.8, 109.6)
- added P309: Conn_01x01_Male, ESP32-HAT:ProtoPad-Drill1mm, F.Cu at (111.8, 107.1)
- added P310: Conn_01x01_Male, ESP32-HAT:ProtoPad-Drill1mm, F.Cu at (124.5, 109.6)
- added P311: Conn_01x01_Male, ESP32-HAT:ProtoPad-Drill1mm, F.Cu at (121.9, 109.6)
- added P312: Conn_01x01_Male, ESP32-HAT:ProtoPad-Drill1mm, F.Cu at (114.3, 107.1)
- added P313: Conn_01x01_Male, ESP32-HAT:ProtoPad-Drill1mm, F.Cu at (119.4, 109.6)
- added P314: Conn_01x01_Male, ESP32-HAT:ProtoPad-Drill1mm, F.Cu at (109.2, 109.6)
- added P315: Conn_01x01_Male, ESP32-HAT:ProtoPad-Drill1mm, F.Cu at (116.8, 107.1)
- added P316: Conn_01x01_Male, ESP32-HAT:ProtoPad-Drill1mm, F.Cu at (111.8, 109.6)
- added P317: Conn_01x01_Male, ESP32-HAT:ProtoPad-Drill1mm, F.Cu at (124.5, 107.1)
- added P318: Conn_01x01_Male, ESP32-HAT:ProtoPad-Drill1mm, F.Cu at (121.9, 107.1)
- added P319: Conn_01x01_Male, ESP32-HAT:ProtoPad-Drill1mm, F.Cu at (114.3, 109.6)
- added P320: Conn_01x01_Male, ESP32-HAT:ProtoPad-Drill1mm, F.Cu at (119.4, 107.1)
- added REF**: THTPad_2.1x2.1mm_Drill1.0mm, SH-ESP32:THTPad_2.1x2.1mm_Drill1.0mm, F.Cu at (167.7, 89.3)
- added REF**: THTPad_2.1x2.1mm_Drill1.0mm, SH-ESP32:THTPad_2.1x2.1mm_Drill1.0mm, F.Cu at (170.2, 96.9)
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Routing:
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
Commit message: Groundpllane on Hat-Proto & moved KeepOut on Blank to user Cmts
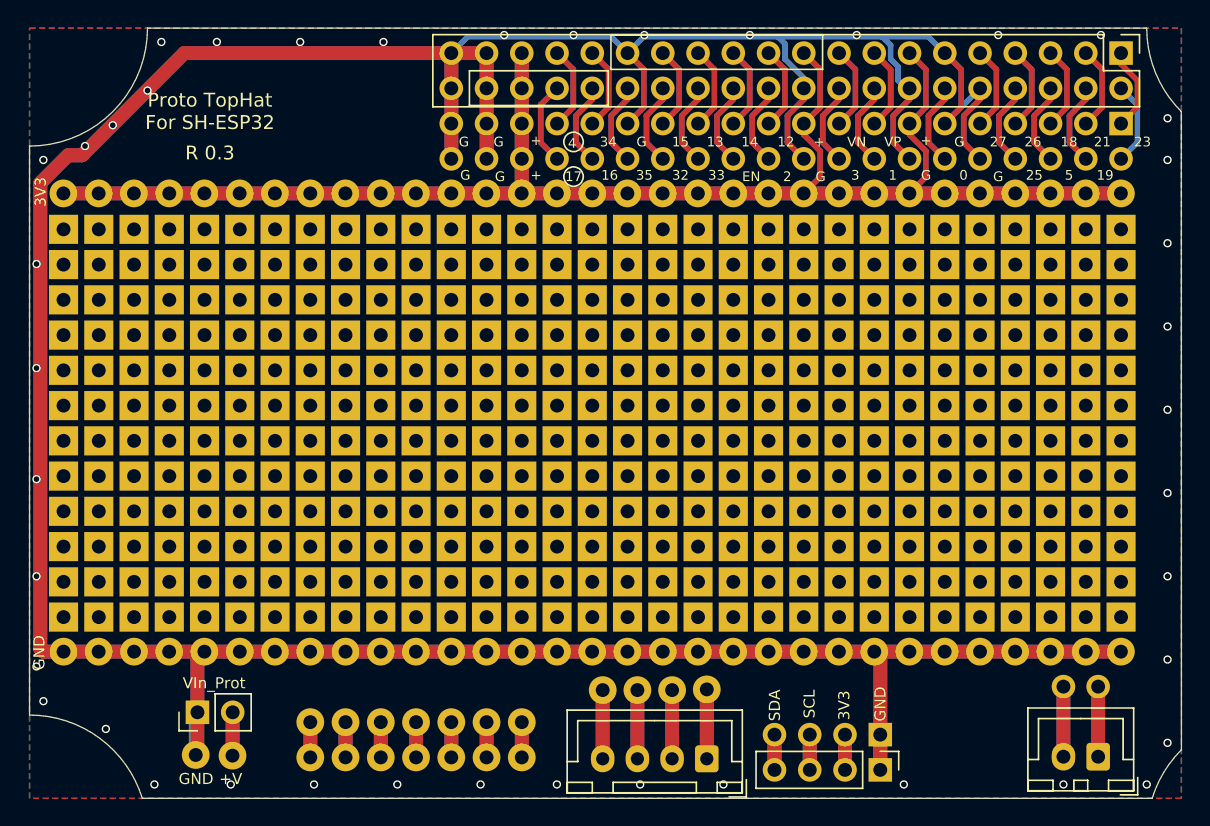
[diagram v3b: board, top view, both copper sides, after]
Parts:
- removed the REF** at (170.2, 96.9)
- removed the REF** at (170.2, 89.3)
- removed the REF** at (170.2, 74.0)
- removed the REF** at (170.2, 76.6)
- removed the REF** at (170.2, 94.4)
- removed the REF** at (170.2, 71.5)
- removed the REF** at (170.2, 91.8)
- removed the REF** at (170.2, 81.7)
- removed the REF** at (170.2, 86.7)
- removed the REF** at (170.2, 69.0)
- removed the REF** at (170.2, 102.0)
- removed the REF** at (170.2, 79.1)
- removed the REF** at (170.2, 99.4)
- removed the REF** at (170.2, 84.2)
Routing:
- net +3V3: track 226.0 -> 220.9 mm
- net GND: track 477.5 -> 472.5 mm, vias 0 -> 42
- added copper zone on B.Cu, net GND
- added copper zone on F.Cu, net GND
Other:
- board text removed: "22"
